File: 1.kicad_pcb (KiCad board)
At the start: 2 copper layers, 85.1 x 46.4 mm, 44 parts, among them J1 Micro_SD_Card, J10 I2C1, J11 I2C2, J12 B3..9A, J2 USB_B_Micro, J3 Conn_Power, J4 SWD, J5 Protected, J6 SPI1, J7 ADC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

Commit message: ops
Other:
- board text added: "3V3 5V"
- board text added: "C D I2C1"
- board text added: "I O K S SPI1"
- board text removed: ". . . . SPI1"
- board text removed: ". . I2C1"
- board text removed: "GND 3V3 5V"
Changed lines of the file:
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@@
   (general
     (thickness 1.6)
-    (drawings 43)
+    (drawings 44)
     (tracks 645)
     (zones 0)
@@
     )
   )
+  (gr_text GND (at 172.72 118.11) (layer Eco2.User)
+    (effects (font (size 1 1) (thickness 0.15)))
+  )
+  (gr_text "I  O K S\nSPI1" (at 160.274 97.79) (layer Eco1.User)
+    (effects (font (size 1.2 1.2) (thickness 0.15)))
+  )
   (gr_text "TIM1\n1  2  3" (at 144.78 126.492) (layer Eco2.User)
-    (effects (font (size 1 1) (thickness 0.15)))
+    (effects (font (size 1 1) (thickness 0.2)))
   )
   (gr_text "TIM2   3   4" (at 113.284 122.174) (layer Eco2.User)
     (effects (font (size 0.8 0.8) (thickness 0.15)))
   )
-  (gr_text ".  .  .  .\nSPI1" (at 115.824 99.314) (layer Eco1.User)
-    (effects (font (size 1.25 1.25) (thickness 0.2)))
+  (gr_text "I  O K S\nSPI1" (at 115.824 100.33) (layer Eco1.User)
+    (effects (font (size 1.05 1.05) (thickness 0.2)))
   )
   (gr_text "UART3  Tx  Rx" (at 113.284 123.444) (layer Eco1.User)
     (effects (font (size 0.8 0.8) (thickness 0.15)))
   )
-  (gr_text ".  .\nI2C1" (at 152.527 97.028) (layer Eco2.User)
+  (gr_text "C  D\nI2C1" (at 152.527 97.79) (layer Eco2.User)
     (effects (font (size 1.25 1.25) (thickness 0.2)))
   )
-  (gr_text "2  1\nTIM2" (at 146.812 90.932) (layer Eco1.User)
+  (gr_text "2  1\nTIM2" (at 147.32 91.186) (layer Eco1.User)
     (effects (font (size 0.8 0.8) (thickness 0.15)) (justify right))
   )
-  (gr_text "GND\n\n\n3V3\n\n\n5V" (at 172.847 123.19) (layer Eco2.User)
+  (gr_text "3V3\n\n\n5V" (at 172.847 125.73) (layer Eco1.User)
     (effects (font (size 1.1 1.1) (thickness 0.2)))
   )
@@
     (effects (font (size 0.8 0.8) (thickness 0.2)))
   )
-  (gr_text "2  1\nTIM3" (at 143.256 90.932) (layer Eco2.User)
+  (gr_text "2  1\nTIM3" (at 143.51 91.186) (layer Eco2.User)
     (effects (font (size 0.8 0.8) (thickness 0.15)) (justify right))
   )
@@
     (effects (font (size 0.65 0.65) (thickness 0.15)))
   )
-  (gr_text "TIM4  2  1\n4  3" (at 136.525 89.535) (layer Eco1.User)
+  (gr_text "TIM4  2  1\n4  3" (at 136.779 89.789) (layer Eco1.User)
     (effects (font (size 0.8 0.8) (thickness 0.15)) (justify left))
-  )
-  (gr_text ".  .  .  .\nSPI1" (at 160.147 97.028) (layer Eco1.User)
-    (effects (font (size 1.25 1.25) (thickness 0.2)))
   )
   (gr_text OSC (at 127 109.982) (layer Dwgs.User)
@@
     (effects (font (size 1.55 1.55) (thickness 0.25)) (justify left))
   )
-  (gr_text "Tx Rx\nUART2" (at 123.571 99.695) (layer Eco1.User)
-    (effects (font (size 1 1) (thickness 0.15)))
+  (gr_text "Tx Rx\nUART2" (at 123.698 100.33) (layer Eco1.User)
+    (effects (font (size 1.05 1.05) (thickness 0.2)))
   )
   (gr_text "A0\nA1\nA2\nA3\nA4\nA5\nA6\nA7\nB0\nB1" (at 118.237 93.98 270) (layer Dwgs.User)
     (effects (font (size 1.5 1.5) (thickness 0.3)))
   )
-  (gr_text "4  3  2  1\nTIM2" (at 126.111 96.901) (layer Eco2.User)
-    (effects (font (size 1 1) (thickness 0.15)))
-  )
-  (gr_text "4  3  2  1\nTIM3" (at 110.617 96.901) (layer Eco2.User)
-    (effects (font (size 1 1) (thickness 0.15)))
+  (gr_text "4  3  2  1\nTIM2" (at 125.984 96.901) (layer Eco2.User)
+    (effects (font (size 1.05 1.05) (thickness 0.2)))
+  )
+  (gr_text "4  3  2  1\nTIM3" (at 110.744 97.028) (layer Eco2.User)
+    (effects (font (size 1.05 1.05) (thickness 0.2)))
   )
   (segment (start 135.656008 130.192212) (end 135.443876 130.192212) (width 0.25) (layer F.Cu) (net 1))
@@
   (segment (start 125.9135 106.1015) (end 125.9135 106.1015) (width 0.25) (layer B.Cu) (net 5))
   (via (at 125.9135 106.1015) (size 0.8) (drill 0.4) (layers F.Cu B.Cu) (net 5))
-  (segment (start 124.900666 107.114334) (end 125.9135 106.1015) (width 0.25) (layer F.Cu) (net 5))
-  (segment (start 124.900666 113.788878) (end 124.900666 107.114334) (width 0.25) (layer F.Cu) (net 5))
-  (segment (start 126.419891 115.308103) (end 124.900666 113.788878) (width 0.25) (layer F.Cu) (net 5))
   (segment (start 126.419891 115.343445) (end 126.419891 115.308103) (width 0.25) (layer F.Cu) (net 5))
+  (segment (start 124.900666 113.82422) (end 126.419891 115.343445) (width 0.25) (layer F.Cu) (net 5))
+  (segment (start 124.900666 107.114334) (end 124.900666 113.82422) (width 0.25) (layer F.Cu) (net 5))
+  (segment (start 125.9135 106.1015) (end 124.900666 107.114334) (width 0.25) (layer F.Cu) (net 5))
   (segment (start 133.934717 119.469322) (end 133.970057 119.469322) (width 0.25) (layer F.Cu) (net 7))
   (segment (start 134.366 96.266) (end 137.871 96.266) (width 0.25) (layer F.Cu) (net 7))
@@
   (segment (start 163.068 109.22) (end 168.91 109.22) (width 0.25) (layer F.Cu) (net 23))
   (segment (start 167.6145 107.9755) (end 167.64 107.95) (width 0.25) (layer F.Cu) (net 24))
-  (segment (start 163.83 107.9755) (end 167.6145 107.9755) (width 0.25) (layer F.Cu) (net 24))
-  (segment (start 163.83 107.9755) (end 163.355 107.9755) (width 0.25) (layer F.Cu) (net 24))
   (segment (start 131.988342 114.636338) (end 137.15068 109.474) (width 0.25) (layer F.Cu) (net 24))
   (segment (start 131.953002 114.636338) (end 131.988342 114.636338) (width 0.25) (layer F.Cu) (net 24))
@@
   (segment (start 139.7 109.474) (end 139.7 109.474) (width 0.25) (layer F.Cu) (net 24))
   (via (at 139.7 109.474) (size 0.8) (drill 0.4) (layers F.Cu B.Cu) (net 24))
-  (segment (start 166.54 107.95) (end 167.64 107.95) (width 0.25) (layer B.Cu) (net 24))
-  (segment (start 166.34399 108.14601) (end 166.54 107.95) (width 0.25) (layer B.Cu) (net 24))
-  (segment (start 141.02799 108.14601) (end 166.34399 108.14601) (width 0.25) (layer B.Cu) (net 24))
-  (segment (start 139.7 109.474) (end 141.02799 108.14601) (width 0.25) (layer B.Cu) (net 24))
+  (segment (start 163.83 107.9755) (end 167.6145 107.9755) (width 0.25) (layer F.Cu) (net 24))
+  (segment (start 140.97 108.204) (end 139.7 109.474) (width 0.25) (layer B.Cu) (net 24))
+  (segment (start 141.02799 108.14601) (end 140.97 108.204) (width 0.25) (layer B.Cu) (net 24))
+  (segment (start 166.31201 108.14601) (end 141.02799 108.14601) (width 0.25) (layer B.Cu) (net 24))
+  (segment (start 166.50802 107.95) (end 166.31201 108.14601) (width 0.25) (layer B.Cu) (net 24))
+  (segment (start 167.64 107.95) (end 166.50802 107.95) (width 0.25) (layer B.Cu) (net 24))
   (via (at 158.4452 105.537) (size 0.8) (drill 0.4) (layers F.Cu B.Cu) (net 25))
   (segment (start 158.445 100.838) (end 158.445 102.87) (width 0.25) (layer F.Cu) (net 25))
   (segment (start 158.445 105.5368) (end 158.4452 105.537) (width 0.25) (layer F.Cu) (net 25))
   (segment (start 158.445 102.87) (end 158.445 105.5368) (width 0.25) (layer F.Cu) (net 25))
-  (segment (start 158.4452 105.537) (end 156.2862 107.696) (width 0.25) (layer B.Cu) (net 25))
   (segment (start 127.619711 113.007731) (end 128.187658 113.575678) (width 0.25) (layer F.Cu) (net 25))
   (segment (start 127.619711 112.641007) (end 127.619711 113.007731) (width 0.25) (layer F.Cu) (net 25))
@@
   (segment (start 131.548718 108.712) (end 131.548718 108.712) (width 0.25) (layer F.Cu) (net 25))
   (via (at 131.548718 108.712) (size 0.8) (drill 0.4) (layers F.Cu B.Cu) (net 25))
+  (segment (start 131.548718 108.712) (end 132.564718 107.696) (width 0.25) (layer B.Cu) (net 25))
+  (segment (start 158.4452 105.537) (end 156.2862 107.696) (width 0.25) (layer B.Cu) (net 25))
   (segment (start 132.564718 107.696) (end 132.588 107.696) (width 0.25) (layer B.Cu) (net 25))
-  (segment (start 131.548718 108.712) (end 132.564718 107.696) (width 0.25) (layer B.Cu) (net 25))
   (segment (start 156.2862 107.696) (end 132.588 107.696) (width 0.25) (layer B.Cu) (net 25))
   (segment (start 119.888 91.44) (end 122.428 88.9) (width 0.25) (layer F.Cu) (net 26))

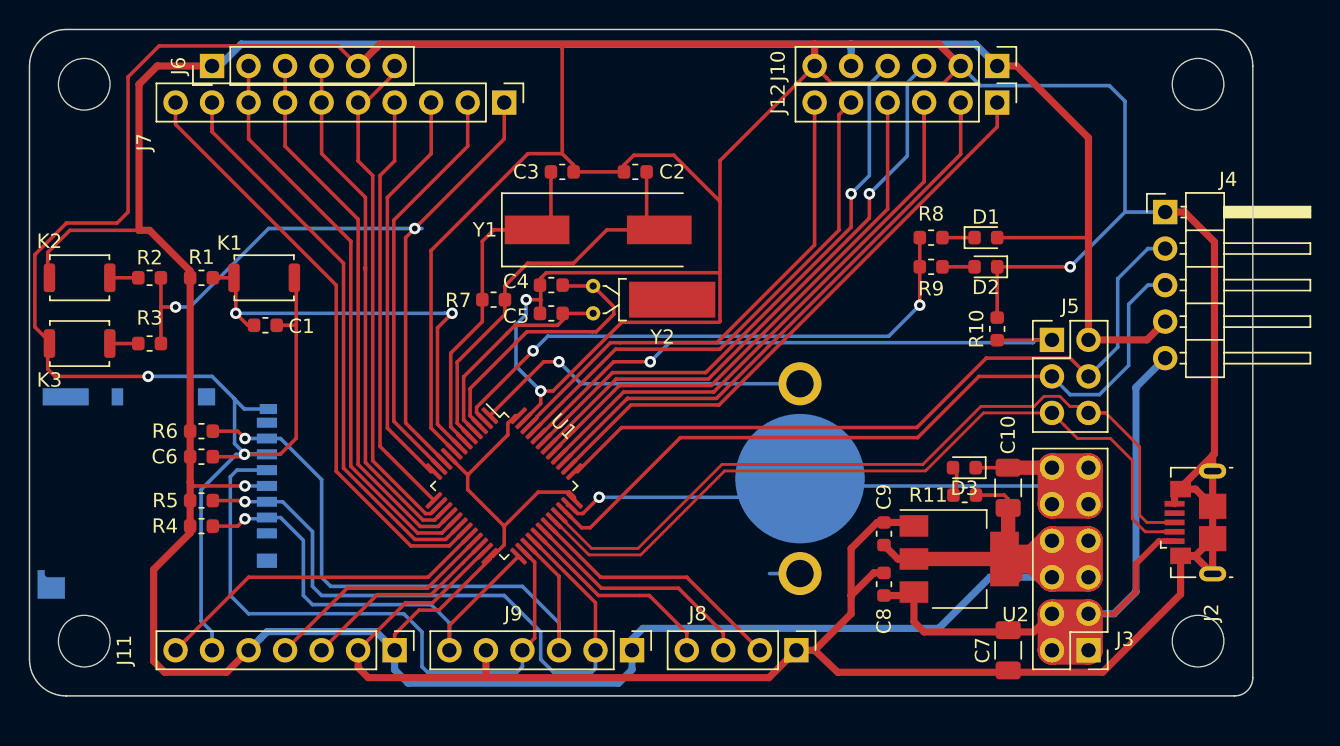
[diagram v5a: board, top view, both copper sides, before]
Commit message: SD ground
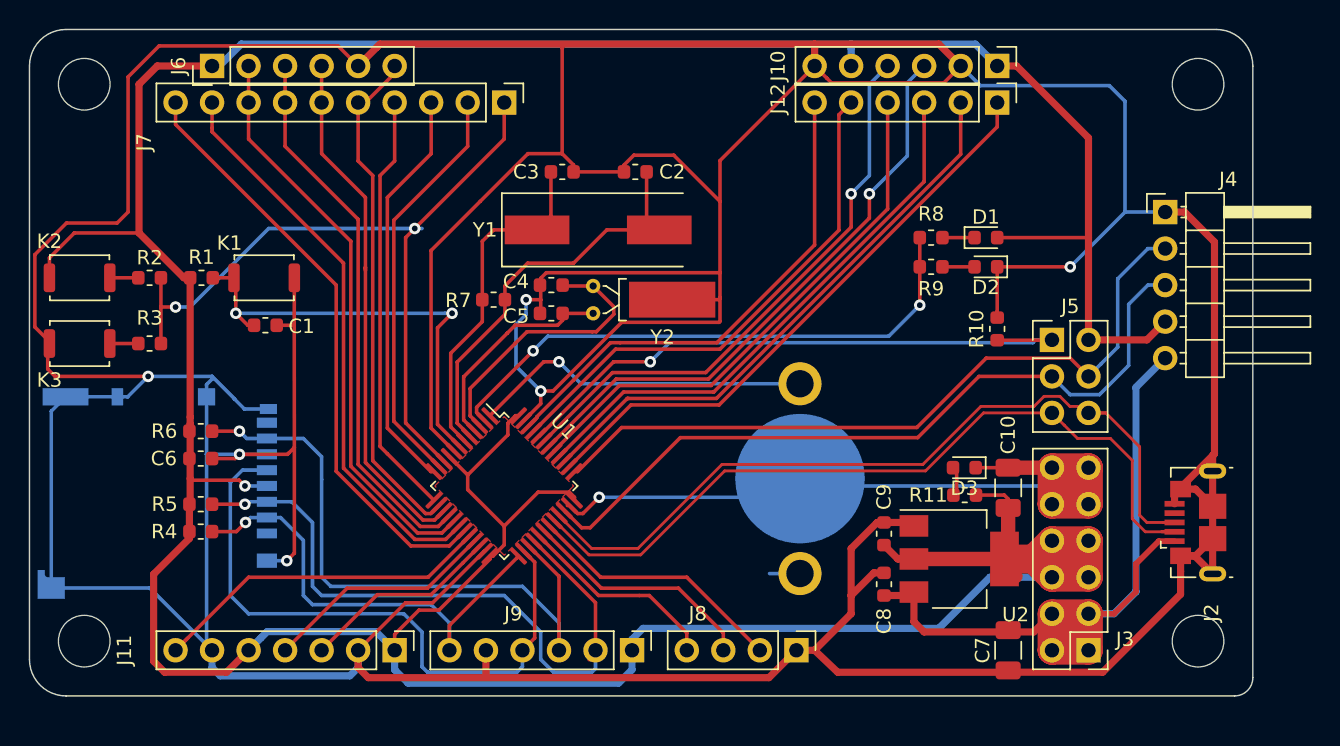
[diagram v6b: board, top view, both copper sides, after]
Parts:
- moved R4 0.38 mm to (108.4, 121.3)
- moved R5 0.26 mm to (108.4, 119.4)
- moved C6 0.14 mm to (108.4, 116.2)
- moved R6 0.05 mm to (108.4, 114.3)
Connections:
- J1 pad 10: (no net) -> GND
- J1 pad 11: (no net) -> GND
- Y2 pad 1: /OSC_32K2 -> /OSC_32K1
- Y2 pad 2: /OSC_32K1 -> /OSC_32K2
- Y2 pad 3: (no net) -> GND
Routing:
- net GND: track 493.5 -> 554.2 mm, vias 6 -> 7
- net /SD_DO: track 43.7 -> 44.6 mm
- added copper zone on F.Cu, net +3V3

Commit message: fix lines
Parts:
- moved C6 0.05 mm to (108.5, 116.2)
- moved R4 0.05 mm to (108.5, 121.3)
- moved R5 0.05 mm to (108.5, 119.4)
- moved R6 0.05 mm to (108.5, 114.3)
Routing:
- net +3V3: track 290.3 -> 291.7 mm
- net GND: track 554.2 -> 552.9 mm

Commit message: fix lines2
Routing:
- net GND: track 552.9 -> 554.5 mm
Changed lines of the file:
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@@
     (thickness 1.6)
     (drawings 44)
-    (tracks 674)
+    (tracks 675)
     (zones 0)
     (modules 44)
@@
   (segment (start 111.506 115.91) (end 108.8408 115.91) (width 0.25) (layer B.Cu) (net 7))
   (segment (start 108.835 111.91) (end 108.835 115.9042) (width 0.25) (layer B.Cu) (net 7))
+  (segment (start 111.506 115.91) (end 113.035 115.91) (width 0.25) (layer B.Cu) (net 7))
   (segment (start 163.83 100.838) (end 170.18 100.838) (width 0.25) (layer F.Cu) (net 8))
   (segment (start 170.18 100.838) (end 170.18 107.95) (width 0.5) (layer F.Cu) (net 8))
